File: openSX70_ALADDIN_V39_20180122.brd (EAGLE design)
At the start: 95.9 x 27.9 mm, 47 parts, among them J1 GND, Q1 5.8A/30V/35mΩ, Q2 5.8A/30V/35mΩ, U1 ATMEGA328P_TQFP, U3 BH1750FVI-TR, Y1 CSTCE16M0V53-R0

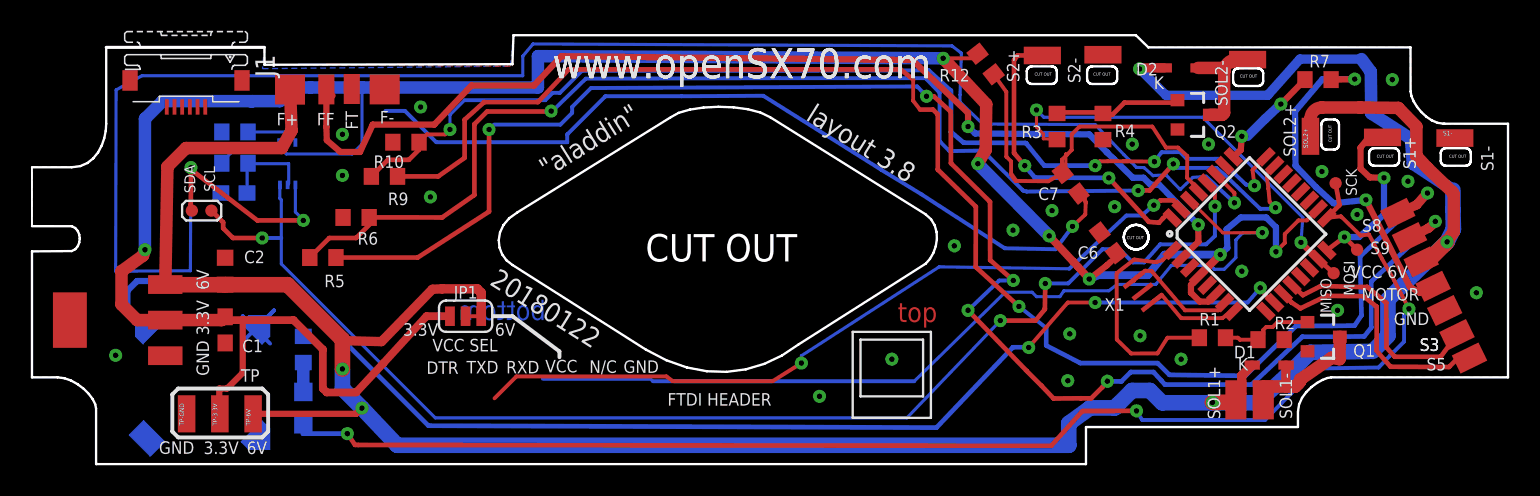
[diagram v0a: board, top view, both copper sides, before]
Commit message: New v.3.9 "Aladdin-fpc" is basically Aladdin with the FTDI header changed to the upper left in the form of a flexible cable.
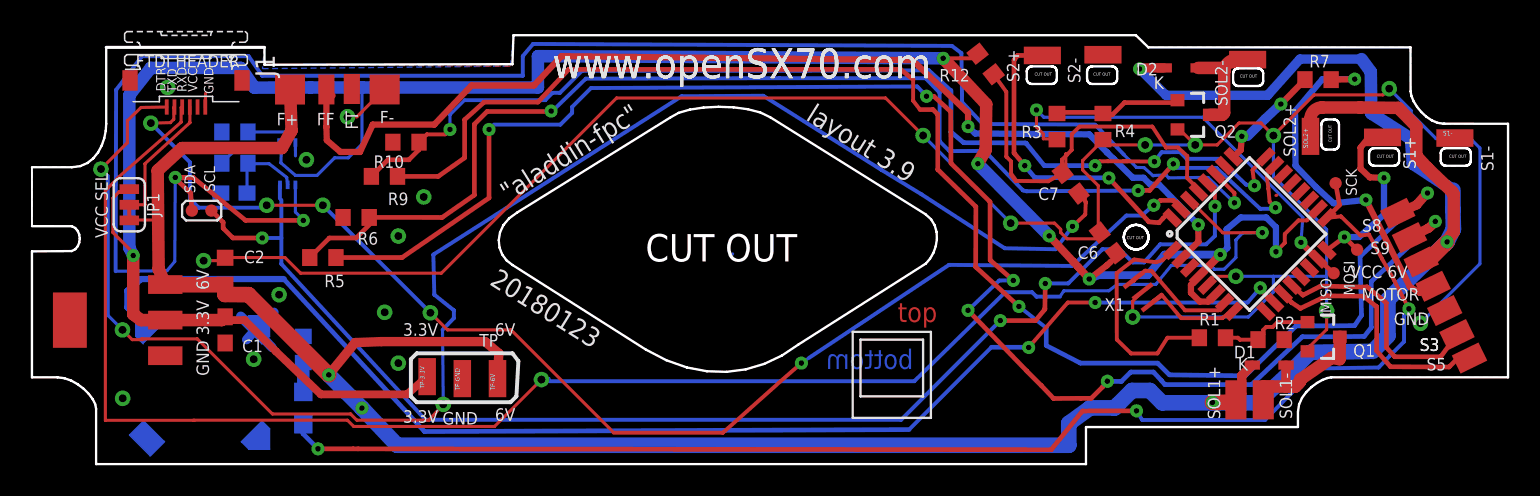
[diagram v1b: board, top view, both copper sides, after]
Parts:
- moved JP1 23.0 mm to (8.38, 17.7), turned to 270 degrees
- moved TP-GND 18.1 mm to (30.1, 6.35)
- moved TP-6V 16.0 mm to (32.4, 6.35)
- moved TP-3.3V 13.7 mm to (27.8, 6.48)
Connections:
- net DTR: now also J1.6; no longer J1.1
- net GND: now also J1.1; no longer J1.6
- net N$27: now also J1.3, JP1.2; no longer J1.4
- net RXD: now also J1.4; no longer J1.3
- net TXD: now also J1.5; no longer J1.2
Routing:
- net GND: track 8.17 -> 165.3 mm, vias 24 -> 21
- net RXD: track 57.5 -> 110.2 mm, vias 1 -> 2
- net DTR: track 54.4 -> 104.2 mm, vias 1 -> 4
- net TXD: track 49.8 -> 84.8 mm, vias 2 -> 6
- net N$27: track 0.00 -> 8.66 mm
- net 3.3V: track 170.4 -> 168.1 mm
- net 6V: track 194.9 -> 193.5 mm
- net N$2: track 6.02 -> 5.29 mm
- net S9@6V: track 106.5 -> 105.9 mm
- net SDA: track 120.8 -> 121.3 mm
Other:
- board text added: ""aladdin-fpc""
- board text added: "20180123"
- board text added: "layout 3.9"
- board text added: "openSX70 project visit www.openSX70.com version 3.9 "aladdin-fpc" 20170123 by Joaquín de Prada"
- board text removed: ""aladdin""
- board text removed: "20180122"
- board text removed: "N/C"
- board text removed: "layout 3.8"
- board text removed: "openSX70 project visit www.openSX70.com version 3.8 "aladdin" 20170122 by Joaquín de Prada"

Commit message: Minor changes to Aladdin-fpc 3.9
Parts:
- moved C1 0.18 mm to (14.7, 9.40)
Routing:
- net TXD: track 84.8 -> 88.8 mm
- net RXD: track 110.2 -> 111.4 mm
- net DTR: track 104.2 -> 103.2 mm
- net GND: vias 21 -> 18
- net 6V: vias 5 -> 4
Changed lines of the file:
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@@
 <attribute name="VALUE" x="6.4671" y="2.4082" size="1.27" layer="28" font="vector" rot="MR90"/>
 </element>
-<element name="C1" library="SparkFun-Capacitors" package="0603" value="10uF" x="14.605" y="9.525" smashed="yes" rot="R90">
-<attribute name="NAME" x="16.383" y="8.89" size="0.8128" layer="25" font="vector" ratio="20" rot="R180" align="bottom-center"/>
-<attribute name="PROD_ID" value="CAP-11015" x="14.605" y="9.525" size="1.778" layer="27" rot="R90" display="off"/>
-<attribute name="VALUE" x="16.891" y="9.779" size="0.8128" layer="27" font="vector" ratio="20" rot="R180" align="top-center"/>
+<element name="C1" library="SparkFun-Capacitors" package="0603" value="10uF" x="14.732" y="9.398" smashed="yes" rot="R90">
+<attribute name="NAME" x="16.51" y="8.763" size="0.8128" layer="25" font="vector" ratio="20" rot="R180" align="bottom-center"/>
+<attribute name="PROD_ID" value="CAP-11015" x="14.732" y="9.398" size="1.778" layer="27" rot="R90" display="off"/>
+<attribute name="VALUE" x="17.018" y="9.652" size="0.8128" layer="27" font="vector" ratio="20" rot="R180" align="top-center"/>
 </element>
 <element name="C2" library="rcl" library_urn="urn:adsk.eagle:library:334" package="C0603K" package3d_urn="urn:adsk.eagle:package:23680/2" value="100nF" x="14.605" y="13.335" smashed="yes" rot="R270">
@@
 <wire x1="80.264" y1="15.367" x2="80.6958" y2="15.81785" width="0.2032" layer="16"/>
 <wire x1="80.6958" y1="15.81785" x2="81.9785" y2="15.84325" width="0.2032" layer="16"/>
-<wire x1="22.5552" y1="3.6576" x2="12.5984" y2="3.6576" width="0.2032" layer="1"/>
-<wire x1="22.9616" y1="3.2512" x2="22.5552" y2="3.6576" width="0.2032" layer="1"/>
-<wire x1="32.1056" y1="3.2512" x2="22.9616" y2="3.2512" width="0.2032" layer="1"/>
+<wire x1="19.3802" y1="2.0066" x2="19.3294" y2="1.8796" width="0.2032" layer="1"/>
+<wire x1="20.50415" y1="3.2258" x2="19.3802" y2="2.0066" width="0.2032" layer="1"/>
+<wire x1="32.1056" y1="3.2512" x2="20.50415" y2="3.2258" width="0.2032" layer="1"/>
 <wire x1="35.1536" y1="6.2992" x2="32.1056" y2="3.2512" width="0.2032" layer="1"/>
 <wire x1="35.1536" y1="6.2992" x2="35.2425" y2="6.35" width="0.2032" layer="16"/>
@@
 <wire x1="6.82625" y1="18.57375" x2="7.62" y2="19.3675" width="0.2032" layer="1"/>
 <wire x1="6.82625" y1="3.65125" x2="6.82625" y2="18.57375" width="0.2032" layer="1"/>
-<wire x1="12.54125" y1="3.65125" x2="6.82625" y2="3.65125" width="0.2032" layer="1"/>
-<wire x1="12.54125" y1="3.65125" x2="12.5984" y2="3.6576" width="0.2032" layer="1"/>
+<wire x1="8.47725" y1="1.87325" x2="6.82625" y2="3.65125" width="0.2032" layer="1"/>
+<wire x1="8.47725" y1="1.87325" x2="19.3294" y2="1.8796" width="0.2032" layer="1"/>
 <wire x1="35.08375" y1="6.35" x2="35.1536" y2="6.2992" width="0.2032" layer="16"/>
 <wire x1="11.7475" y1="23.01875" x2="11.7475" y2="23.97125" width="0.2032" layer="1"/>
@@
 <via x="74.93" y="17.62125" extent="1-16" drill="0.35"/>
 <via x="52.03825" y="7.366" extent="1-16" drill="0.35"/>
-<wire x1="50.546" y1="6.06425" x2="52.03825" y2="7.366" width="0.254" layer="1"/>
-<wire x1="46.9392" y1="2.8448" x2="39.84625" y2="2.8448" width="0.254" layer="1"/>
-<wire x1="50.4444" y1="5.969" x2="46.9392" y2="2.8448" width="0.254" layer="1"/>
-<wire x1="50.4444" y1="5.969" x2="50.546" y2="6.06425" width="0.2032" layer="1"/>
+<wire x1="53.2511" y1="5.91185" x2="52.03825" y2="7.366" width="0.254" layer="1"/>
+<wire x1="52.5526" y1="2.86385" x2="40.35425" y2="2.8448" width="0.254" layer="1"/>
+<wire x1="53.2384" y1="3.81" x2="52.5526" y2="2.86385" width="0.254" layer="1"/>
+<wire x1="53.2384" y1="3.81" x2="53.2511" y2="5.91185" width="0.2032" layer="1"/>
 <contactref element="J1" pad="5"/>
 <wire x1="11.27125" y1="23.20925" x2="11.27125" y2="23.97125" width="0.2032" layer="1"/>
@@
 <wire x1="39.84625" y1="2.8575" x2="33.17875" y2="9.525" width="0.2032" layer="1"/>
 <wire x1="11.27125" y1="23.97125" x2="11.315" y2="24.003" width="0.2032" layer="1"/>
-<wire x1="39.84625" y1="2.8575" x2="39.84625" y2="2.8448" width="0.2032" layer="1"/>
+<wire x1="39.84625" y1="2.8575" x2="40.35425" y2="2.8448" width="0.2032" layer="1"/>
 <via x="9.779" y="22.95525" extent="1-16" drill="0.508"/>
 <via x="17.30375" y="17.62125" extent="1-16" drill="0.508"/>
@@
 <wire x1="15.9385" y1="16.637" x2="19.685" y2="16.637" width="0.3048" layer="1"/>
 <contactref element="SDA" pad="TP"/>
-<wire x1="12.446" y1="17.272" x2="12.3698" y2="18.40865" width="0.3048" layer="1"/>
+<wire x1="12.446" y1="17.272" x2="12.42695" y2="18.3896" width="0.3048" layer="1"/>
 <wire x1="11.374109375" y1="19.362409375" x2="12.514115625" y2="19.432259375" width="0.3048" layer="1"/>
-<wire x1="12.3698" y1="18.40865" x2="11.374109375" y2="19.362409375" width="0.3048" layer="1"/>
+<wire x1="12.42695" y1="18.3896" x2="11.374109375" y2="19.362409375" width="0.3048" layer="1"/>
 </signal>
 <signal name="3.3V">
@@
 <via x="68.1355" y="15.6337" extent="1-16" drill="0.35"/>
 <wire x1="10.7188" y1="10.16" x2="14.39" y2="10.16" width="0.8128" layer="1"/>
-<wire x1="14.39" y1="10.16" x2="14.605" y2="10.375" width="0.8128" layer="1"/>
+<wire x1="14.39" y1="10.16" x2="14.732" y2="10.248" width="0.8128" layer="1"/>
 <wire x1="10.7188" y1="10.16" x2="15.875" y2="10.16" width="0.508" layer="1"/>
 <wire x1="17.907" y1="8.128" x2="20.828" y2="5.334" width="0.508" layer="1"/>
@@
 <wire x1="96.1136" y1="13.8176" x2="96.1136" y2="21.336" width="0.2032" layer="16"/>
 <wire x1="92.2528" y1="9.9568" x2="96.1136" y2="13.8176" width="0.2032" layer="16"/>
-<via x="13.208" y="14.0208" extent="1-16" drill="0.508"/>
 <via x="22.5552" y="23.368" extent="1-16" drill="0.508"/>
 <via x="59.944" y="22.1488" extent="1-16" drill="0.508"/>
@@
 <via x="24.9682" y="10.668" extent="1-16" drill="0.508"/>
 <via x="16.4592" y="7.62" extent="1-16" drill="0.508"/>
-<via x="7.9502" y="5.08" extent="1-16" drill="0.508"/>
 <via x="19.8882" y="20.574" extent="1-16" drill="0.508"/>
-<via x="25.8572" y="15.621" extent="1-16" drill="0.508"/>
-<via x="27.5082" y="18.161" extent="1-16" drill="0.508"/>
 <wire x1="19.169" y1="21.695" x2="19.177" y2="20.828" width="0.2032" layer="16"/>
 <via x="10.8712" y="25.273" extent="1-16" drill="0.508"/>
@@
 <via x="18.1102" y="11.811" extent="1-16" drill="0.508"/>
 <wire x1="13.315" y1="24.003" x2="13.335" y2="24.892" width="0.2032" layer="1"/>
+<via x="36.7792" y="7.874" extent="1-16" drill="0.508"/>
 </signal>
 <signal name="6V">
@@
 <contactref element="D1" pad="1"/>
 <contactref element="TP-6V" pad="P$1"/>
-<via x="23.495" y="4.445" extent="1-16" drill="0.35"/>
 <wire x1="73.5143625" y1="5.588" x2="72.62025625" y2="4.69389375" width="1.016" layer="16"/>
 <wire x1="72.62025625" y1="4.69389375" x2="72.36625625" y2="4.4583" width="1.016" layer="16"/>
@@
 <wire x1="29.464" y1="10.287" x2="28.7274" y2="9.525" width="0.254" layer="16"/>
 <wire x1="28.1305" y1="14.4145" x2="28.194" y2="11.811" width="0.254" layer="16"/>
-<wire x1="12.8016" y1="8.9408" x2="9.2075" y2="8.9408" width="0.2032" layer="1"/>
+<wire x1="12.5476" y1="8.9408" x2="9.2075" y2="8.9408" width="0.2032" layer="1"/>
 <wire x1="9.2075" y1="8.9408" x2="9.144" y2="8.9408" width="0.2032" layer="1"/>
-<wire x1="17.6784" y1="4.064" x2="12.8016" y2="8.9408" width="0.2032" layer="1"/>
-<wire x1="22.7584" y1="4.064" x2="17.6784" y2="4.064" width="0.2032" layer="1"/>
-<wire x1="23.1648" y1="3.6576" x2="22.7584" y2="4.064" width="0.2032" layer="1"/>
-<wire x1="27.8384" y1="3.6576" x2="23.1648" y2="3.6576" width="0.2032" layer="1"/>
-<wire x1="28.7782" y1="4.6863" x2="27.8384" y2="3.6576" width="0.2032" layer="1"/>
+<wire x1="15.2654" y1="6.223" x2="12.5476" y2="8.9408" width="0.2032" layer="1"/>
+<wire x1="18.1864" y1="6.223" x2="15.2654" y2="6.223" width="0.2032" layer="1"/>
+<wire x1="20.3454" y1="4.66725" x2="18.1864" y2="6.223" width="0.2032" layer="1"/>
+<wire x1="27.7114" y1="4.6736" x2="20.3454" y2="4.66725" width="0.2032" layer="1"/>
+<wire x1="28.7782" y1="4.6863" x2="27.7114" y2="4.6736" width="0.2032" layer="1"/>
 <wire x1="28.7274" y1="9.525" x2="28.7782" y2="4.6863" width="0.2032" layer="16"/>
 <via x="28.7782" y="4.6863" extent="1-16" drill="0.508"/>
@@
 <via x="71.91481875" y="6.190184375" extent="1-16" drill="0.35"/>
 <wire x1="71.91481875" y1="6.190184375" x2="71.595184375" y2="5.809184375" width="0.3048" layer="1"/>
-<wire x1="71.595184375" y1="5.809184375" x2="70.866" y2="5.08" width="0.3048" layer="1"/>
-<wire x1="70.866" y1="5.08" x2="70.19925" y2="5.08" width="0.3048" layer="1"/>
-<wire x1="70.19925" y1="5.08" x2="68.42125" y2="5.0673" width="0.3048" layer="1"/>
-<wire x1="68.42125" y1="5.0673" x2="67.6275" y2="5.9055" width="0.3048" layer="1"/>
+<wire x1="71.595184375" y1="5.809184375" x2="71.12" y2="5.334" width="0.3048" layer="1"/>
+<wire x1="71.12" y1="5.334" x2="70.19925" y2="5.334" width="0.3048" layer="1"/>
+<wire x1="70.19925" y1="5.334" x2="68.16725" y2="5.3213" width="0.3048" layer="1"/>
+<wire x1="68.16725" y1="5.3213" x2="67.6275" y2="5.9055" width="0.3048" layer="1"/>
 <wire x1="67.6275" y1="5.9055" x2="66.675" y2="6.858" width="0.3048" layer="1"/>
 <wire x1="66.675" y1="6.858" x2="62.865" y2="10.795" width="0.3048" layer="1"/>

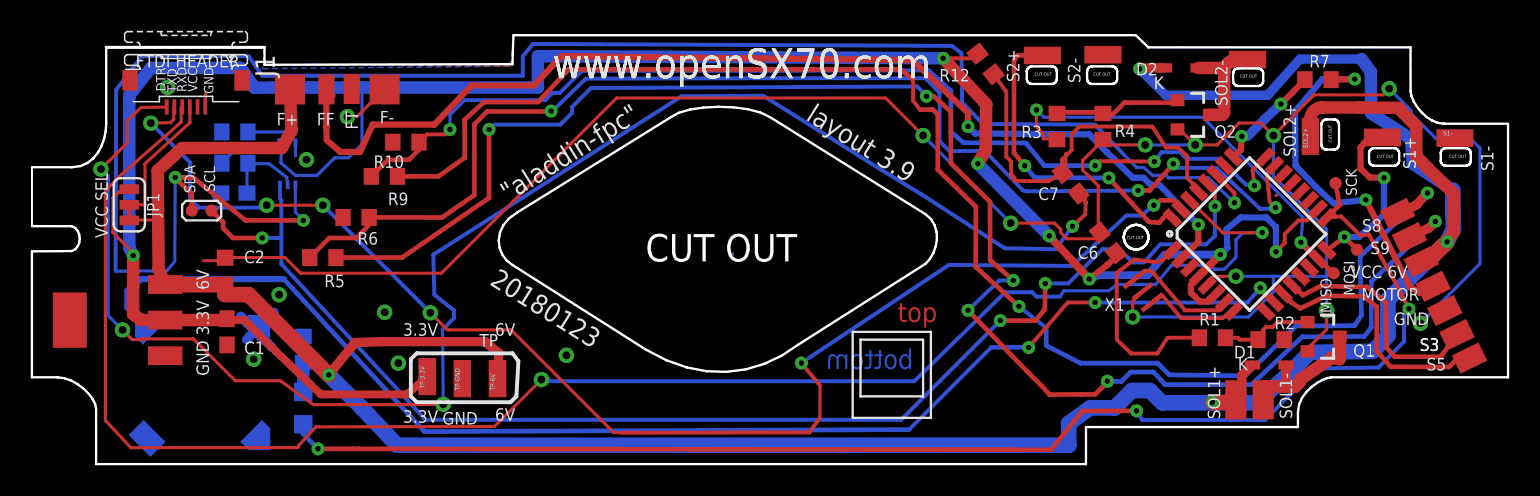
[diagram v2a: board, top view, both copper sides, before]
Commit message: Minor  changed to v.3.9 FPC with a flat cable .5mm for the FTDI. It is a variant based on the Aladdin v3.8
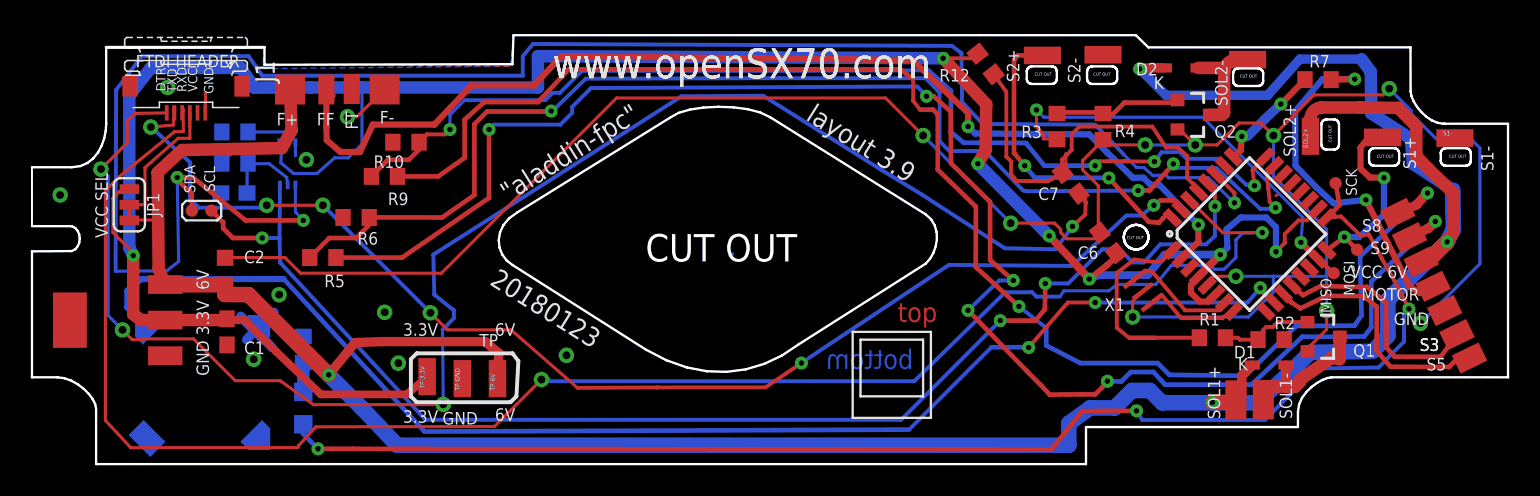
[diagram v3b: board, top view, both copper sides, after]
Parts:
- moved J1 0.38 mm to (12.1, 25.5)
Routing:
- net TXD: track 88.8 -> 82.6 mm
- net SOL1: track 14.8 -> 16.6 mm
- net GND: track 165.3 -> 164.4 mm, vias 18 -> 19

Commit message: Fixing little things in all Aladdin boards
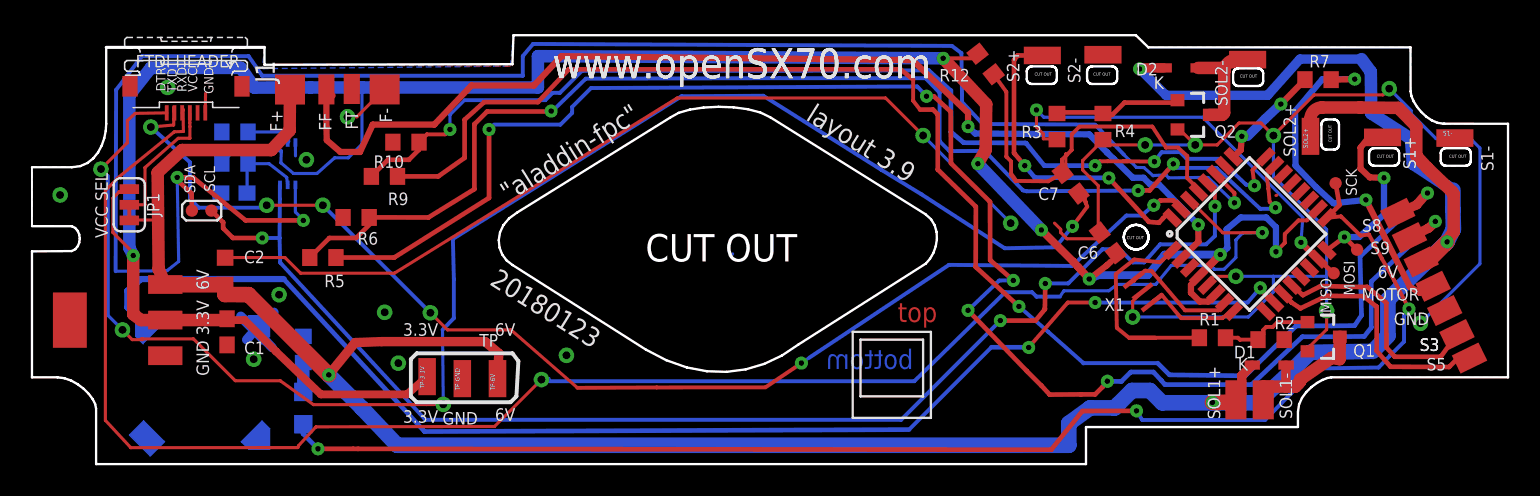
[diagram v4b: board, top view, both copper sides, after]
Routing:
- net GND: track 164.4 -> 160.1 mm
- net DTR: track 103.0 -> 101.7 mm
- net S8@6V: track 94.5 -> 94.0 mm
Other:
- board text removed: "VCC 6V"

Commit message: Minor retouches
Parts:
- moved MISO 2.16 mm to (88.1, 14.7), turned to 90 degrees
- moved MOSI 2.16 mm to (86.6, 13.2), turned to 0 degrees
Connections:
- net S1: now also MISO.TP; no longer MOSI.TP
- net SOL2: now also MOSI.TP; no longer MISO.TP
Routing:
- net 6V: track 193.1 -> 192.4 mm
- net SDA: track 121.4 -> 120.8 mm
